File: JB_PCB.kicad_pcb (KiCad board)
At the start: 2 copper layers, 66 x 102.2 mm, 13 parts, among them J2 Screw_Terminal_01x02, J3 Screw_Terminal_01x02, J4 Screw_Terminal_01x02, J6 Screw_Terminal_01x02

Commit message: Added Servo pins
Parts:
- added J1: Conn_01x03_Pin, myFootprints.pretty-master:3x1_Pin_Header, F.Cu at (149.0, 141.2)
- added J5: Conn_01x03_Pin, myFootprints.pretty-master:3x1_Pin_Header, F.Cu at (152.5, 141.2)
- added J7: Conn_01x03_Pin, myFootprints.pretty-master:3x1_Pin_Header, F.Cu at (156.0, 141.2)
- added J8: Conn_01x03_Pin, myFootprints.pretty-master:3x1_Pin_Header, F.Cu at (159.5, 141.2)
- added J9: Conn_01x03_Pin, myFootprints.pretty-master:3x1_Pin_Header, F.Cu at (163.0, 141.2)
- moved REF** 13.6 mm to (159.5, 152.5)
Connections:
- A1 pad 10: unconnected-(A1-D7-Pad10) -> Net-(A1-D7)
- A1 pad 11: unconnected-(A1-D8-Pad11) -> Net-(A1-D8)
- A1 pad 16: unconnected-(A1-D13-Pad16) -> Net-(A1-D13)
- A1 pad 5: unconnected-(A1-D2-Pad5) -> Net-(A1-D2)
- A1 pad 7: unconnected-(A1-D4-Pad7) -> Net-(A1-D4)
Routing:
- net Net-(A1-D7): track 0.00 -> 83.6 mm
- net Net-(A1-D13): track 0.00 -> 81.9 mm, vias 0 -> 1
- net Net-(A1-D8): track 0.00 -> 73.9 mm, vias 0 -> 2
- net Net-(A1-VIN): track 37.6 -> 100.2 mm, vias 0 -> 1
- net Net-(A1-D4): track 0.00 -> 60.2 mm
- net Net-(A1-D2): track 0.00 -> 54.5 mm
- net Net-(ARD_PWR1-Pin_1): track 121.9 -> 164.6 mm
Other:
- board size 66 x 102.2 mm -> 66 x 114.2 mm
- board text added: "D13"
- board text added: "D2"
- board text added: "D4"
- board text added: "D7"
- board text added: "SIG"
- board text added: "TigerSharks R.O.V. CO"

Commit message: thickened traces
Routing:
- net Net-(J2-Pin_2): track 139.6 -> 145.7 mm
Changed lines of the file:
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@@
 		(descr "<B>WR-PHD </B><BR> 2.54mm Pin Header, 3 Pin")
 		(property "Reference" "J1"
-			(at -6.6096 -0.6625 270)
+			(at -6.6096 -0.6625 -90)
 			(layer "F.SilkS")
 			(hide yes)
@@
 		)
 		(property "Value" "Conn_01x03_Pin"
-			(at -8.968 1.0378 270)
+			(at -8.968 1.0378 -90)
 			(layer "F.Fab")
 			(effects
@@
 		(descr "<B>WR-PHD </B><BR> 2.54mm Pin Header, 3 Pin")
 		(property "Reference" "J8"
-			(at -6.6096 -0.6625 270)
+			(at -6.6096 -0.6625 -90)
 			(layer "F.SilkS")
 			(hide yes)
@@
 		)
 		(property "Value" "Conn_01x03_Pin"
-			(at -8.968 1.0378 270)
+			(at -8.968 1.0378 -90)
 			(layer "F.Fab")
 			(effects
@@
 		(descr "<B>WR-PHD </B><BR> 2.54mm Pin Header, 3 Pin")
 		(property "Reference" "J9"
-			(at -6.6096 -0.6625 270)
+			(at -6.6096 -0.6625 -90)
 			(layer "F.SilkS")
 			(hide yes)
@@
 		)
 		(property "Value" "Conn_01x03_Pin"
-			(at -8.968 1.0378 270)
+			(at -8.968 1.0378 -90)
 			(layer "F.Fab")
 			(effects
@@
 		(descr "<B>WR-PHD </B><BR> 2.54mm Pin Header, 3 Pin")
 		(property "Reference" "J5"
-			(at -6.6096 -0.6625 270)
+			(at -6.6096 -0.6625 -90)
 			(layer "F.SilkS")
 			(hide yes)
@@
 		)
 		(property "Value" "Conn_01x03_Pin"
-			(at -8.968 1.0378 270)
+			(at -8.968 1.0378 -90)
 			(layer "F.Fab")
 			(effects
@@
 		(descr "<B>WR-PHD </B><BR> 2.54mm Pin Header, 3 Pin")
 		(property "Reference" "J7"
-			(at -6.6096 -0.6625 270)
+			(at -6.6096 -0.6625 -90)
 			(layer "F.SilkS")
 			(hide yes)
@@
 		)
 		(property "Value" "Conn_01x03_Pin"
-			(at -8.968 1.0378 270)
+			(at -8.968 1.0378 -90)
 			(layer "F.Fab")
 			(effects
@@
 		(start 110.250004 131.25)
 		(end 110.25 131.25)
-		(width 0.8)
-		(layer "F.Cu")
-		(net 29)
-	)
-	(segment
-		(start 112 138.75)
-		(end 135.104898 138.75)
-		(width 0.8)
+		(width 3.81)
 		(layer "F.Cu")
 		(net 29)
@@
 		(start 109.5 131.25)
 		(end 109.5 109.75)
-		(width 0.8)
+		(width 3.81)
 		(layer "F.Cu")
 		(net 29)
@@
 		(start 115.5 81.500004)
 		(end 110.000004 87)
-		(width 0.8)
+		(width 3.81)
 		(layer "F.Cu")
 		(net 29)
@@
 		(start 109.5 65.250008)
 		(end 115.5 59.250008)
-		(width 0.8)
+		(width 3.81)
 		(layer "F.Cu")
 		(net 29)
@@
 		(start 115.5 103.645106)
 		(end 109.5 109.645106)
-		(width 0.8)
+		(width 3.81)
 		(layer "F.Cu")
 		(net 29)
@@
 		(start 109.5 109.75)
 		(end 109.5 87)
-		(width 0.8)
+		(width 3.81)
 		(layer "F.Cu")
 		(net 29)
@@
 		(start 109.5 132)
 		(end 109.5 131.25)
-		(width 0.8)
+		(width 3.81)
 		(layer "F.Cu")
 		(net 29)
 	)
 	(segment
-		(start 135.104898 138.75)
-		(end 140.854898 133)
-		(width 0.8)
+		(start 109.5 139.5)
+		(end 113.75 143.75)
+		(width 3.81)
 		(layer "F.Cu")
 		(net 29)
 	)
 	(segment
-		(start 109.5 132)
-		(end 109.5 136.25)
-		(width 0.8)
+		(start 113.75 143.75)
+		(end 130.104898 143.75)
+		(width 3.81)
 		(layer "F.Cu")
 		(net 29)
@@
 		(start 110.25 131.25)
 		(end 109.5 132)
-		(width 0.8)
+		(width 3.81)
 		(layer "F.Cu")
 		(net 29)
 	)
 	(segment
-		(start 109.5 136.25)
-		(end 112 138.75)
-		(width 0.8)
+		(start 130.104898 143.75)
+		(end 140.854898 133)
+		(width 3.81)
 		(layer "F.Cu")
 		(net 29)
@@
 		(start 110.000004 87)
 		(end 109.5 87)
-		(width 0.8)
+		(width 3.81)
 		(layer "F.Cu")
 		(net 29)
@@
 		(start 115.5 126.000004)
 		(end 110.250004 131.25)
-		(width 0.8)
+		(width 3.81)
 		(layer "F.Cu")
 		(net 29)
@@
 		(start 109.5 87)
 		(end 109.5 65.250008)
-		(width 0.8)
+		(width 3.81)
+		(layer "F.Cu")
+		(net 29)
+	)
+	(segment
+		(start 109.5 132)
+		(end 109.5 139.5)
+		(width 3.81)
 		(layer "F.Cu")
 		(net 29)
@@
 		(start 109.5 109.645106)
 		(end 109.5 109.75)
-		(width 0.8)
+		(width 3.81)
 		(layer "F.Cu")
 		(net 29)
@@
 		(start 125.75 133)
 		(end 118 133)
-		(width 0.8)
+		(width 3.81)
 		(layer "F.Cu")
 		(net 30)
@@
 		(start 125.75 133)
 		(end 121.25 128.5)
-		(width 0.8)
+		(width 3.81)
 		(layer "F.Cu")
 		(net 30)
@@
 		(start 121.25 71)
 		(end 119.000004 68.750004)
-		(width 0.8)
+		(width 3.81)
 		(layer "F.Cu")
 		(net 30)
@@
 		(start 119.000004 68.750004)
 		(end 115.5 68.750004)
-		(width 0.8)
+		(width 3.81)
 		(layer "F.Cu")
 		(net 30)
@@
 		(start 131.354902 133)
 		(end 125.75 133)
-		(width 0.8)
+		(width 3.81)
 		(layer "F.Cu")
 		(net 30)
@@
 		(start 119.145102 113.145102)
 		(end 121.25 115.25)
-		(width 0.8)
+		(width 3.81)
 		(layer "F.Cu")
 		(net 30)
@@
 		(start 121.25 115.25)
 		(end 121.25 128.5)
-		(width 0.8)
+		(width 3.81)
 		(layer "F.Cu")
 		(net 30)
@@
 		(start 115.5 91)
 		(end 119 91)
-		(width 0.8)
+		(width 3.81)
 		(layer "F.Cu")
 		(net 30)
@@
 		(start 121.25 71)
 		(end 121.25 93.25)
-		(width 0.8)
+		(width 3.81)
 		(layer "F.Cu")
 		(net 30)
@@
 		(start 121.25 93.25)
 		(end 121.25 115.25)
-		(width 0.8)
+		(width 3.81)
 		(layer "F.Cu")
 		(net 30)
@@
 		(start 115.5 113.145102)
 		(end 119.145102 113.145102)
-		(width 0.8)
+		(width 3.81)
 		(layer "F.Cu")
 		(net 30)
@@
 		(start 119 91)
 		(end 121.25 93.25)
-		(width 0.8)
+		(width 3.81)
 		(layer "F.Cu")
 		(net 30)
@@
 		(start 118 133)
 		(end 115.5 135.5)
-		(width 0.8)
+		(width 3.81)
 		(layer "F.Cu")
 		(net 30)

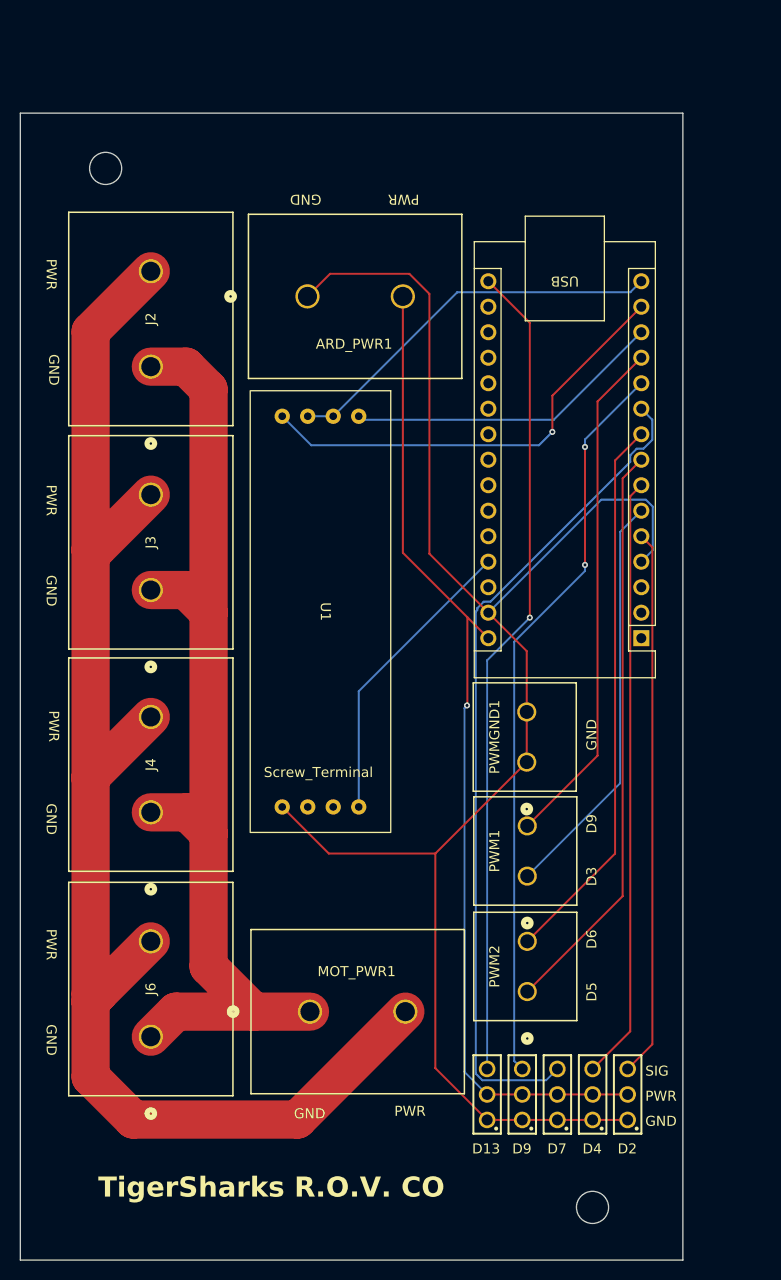
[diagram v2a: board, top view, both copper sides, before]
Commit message: added pins for external PWM board
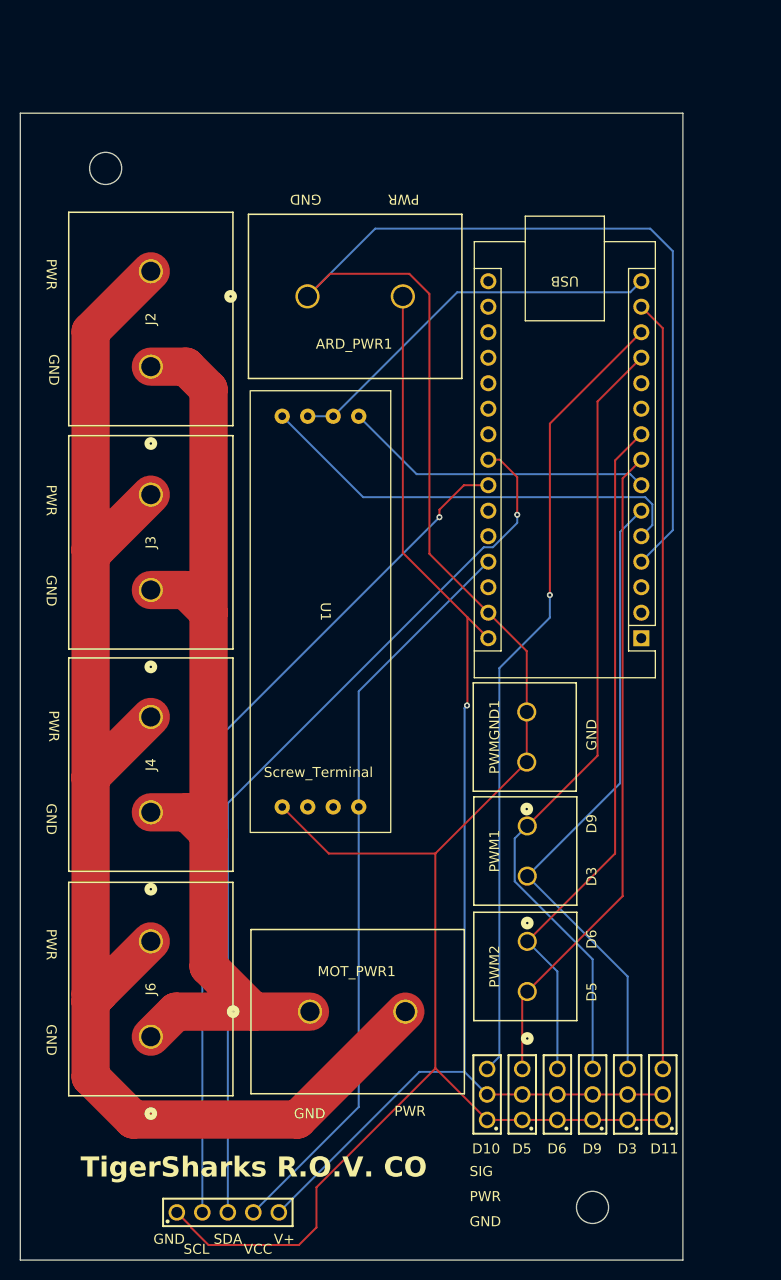
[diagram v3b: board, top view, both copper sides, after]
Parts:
- added J10: Conn_01x03_Pin, myFootprints.pretty-master:3x1_Pin_Header, F.Cu at (166.5, 141.2)
- added J12: Conn_01x05_Pin, myFootprints.pretty-master:1x5conn, F.Cu at (123.2, 153.0)
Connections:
- A1 pad 10: Net-(A1-D7) -> unconnected-(A1-D7-Pad10)
- A1 pad 11: Net-(A1-D8) -> unconnected-(A1-D8-Pad11)
- A1 pad 16: Net-(A1-D13) -> unconnected-(A1-D13-Pad16)
- A1 pad 23: unconnected-(A1-A4-Pad23) -> Net-(A1-A4)
- A1 pad 24: unconnected-(A1-A5-Pad24) -> Net-(A1-A5)
- J1 pad 3: Net-(A1-D13) -> Net-(A1-D10)
- J5 pad 3: Net-(A1-D8) -> Net-(A1-D5)
- J7 pad 3: Net-(A1-D7) -> Net-(A1-D6)
- J8 pad 3: Net-(A1-D4) -> Net-(A1-D9)
- J9 pad 3: Net-(A1-D2) -> Net-(A1-D3)
- U1 pad DI: Net-(A1-D11) -> Net-(A1-D2)
- U1 pad RO: Net-(A1-D10) -> Net-(A1-D4)
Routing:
- net Net-(A1-A4): track 0.00 -> 89.3 mm, vias 0 -> 1
- net Net-(A1-A5): track 0.00 -> 85.7 mm, vias 0 -> 1
- net Net-(ARD_PWR1-Pin_1): track 164.6 -> 250.0 mm
- net Net-(A1-D7): track 83.6 -> 0.00 mm
- net Net-(A1-D13): track 81.9 -> 0.00 mm, vias 1 -> 0
- net Net-(A1-D8): track 73.9 -> 0.00 mm, vias 2 -> 0
- net Net-(A1-D10): track 31.9 -> 79.8 mm, vias 0 -> 1
- net Net-(A1-+5V): track 29.8 -> 74.5 mm
- net Net-(A1-D11): track 44.8 -> 76.8 mm, vias 1 -> 0
- net Net-(A1-D4): track 60.2 -> 31.0 mm
- net Net-(A1-D9): track 51.3 -> 79.3 mm
- net Net-(A1-VIN): track 100.2 -> 128.0 mm
- net Net-(A1-D3): track 41.1 -> 64.5 mm
- net Net-(A1-D6): track 55.2 -> 69.2 mm
- net Net-(A1-D2): track 54.5 -> 44.1 mm
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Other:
- board text added: "D10"
- board text added: "D11"
- board text added: "SCL"
- board text added: "SDA"
- board text added: "V+"
- board text added: "VCC"
- board text removed: "D13"
- board text removed: "D2"
- board text removed: "D4"
- board text removed: "D7"

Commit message: changes from my laptop from last year
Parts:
- removed J10, J5, J7, J8, J9: Conn_01x03_Pin, myFootprints.pretty-master:3x1_Pin_Header
- removed J12: Conn_01x05_Pin, myFootprints.pretty-master:1x5conn
- removed PWM1, PWM2, PWMGND1: Screw_Terminal_01x02, myFootprints.pretty-master:screw 2x2
- added G***: LOGO, myFootprints.pretty-master:MateLogo, F.Cu at (142.5, 150.5)
- added REF**: CON6_1X6_TU_HTS_SAI, myFootprints.pretty-master:1x6Headers, F.Cu at (161.2, 144.0)
- J1: value Conn_01x03_Pin -> Conn_01x06_Pin; footprint myFootprints.pretty-master:3x1_Pin_Header -> myFootprints.pretty-master:1x6Headers
- moved J1 57.0 mm to (161.2, 85.5), turned to 0 degrees
- moved A1 17.9 mm to (165.0, 77.9)
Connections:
- A1 pad 11: unconnected-(A1-D8-Pad11) -> Net-(A1-D8)
- A1 pad 12: Net-(A1-D9) -> unconnected-(A1-D9-Pad12)
- A1 pad 13: Net-(A1-D10) -> unconnected-(A1-D10-Pad13)
- A1 pad 14: Net-(A1-D11) -> unconnected-(A1-D11-Pad14)
- A1 pad 16: unconnected-(A1-D13-Pad16) -> Net-(A1-D13)
- A1 pad 27: Net-(A1-+5V) -> Net-(A1-VIN)
- A1 pad 4: Net-(ARD_PWR1-Pin_1) -> unconnected-(A1-GND-Pad4)
- A1 pad 5: Net-(A1-D2) -> unconnected-(A1-D2-Pad5)
- A1 pad 6: Net-(A1-D3) -> unconnected-(A1-D3-Pad6)
- A1 pad 7: Net-(A1-D4) -> unconnected-(A1-D4-Pad7)
- A1 pad 8: Net-(A1-D5) -> unconnected-(A1-D5-Pad8)
- A1 pad 9: Net-(A1-D6) -> unconnected-(A1-D6-Pad9)
- J1 pad 2: Net-(A1-VIN) -> unconnected-(J1-Pin_2-Pad2)
- J1 pad 3: Net-(A1-D10) -> Net-(A1-A5)
- U1 pad DE: Net-(A1-D12) -> Net-(A1-D13)
- U1 pad DI: Net-(A1-D2) -> Net-(A1-D12)
- U1 pad RE: Net-(A1-D12) -> Net-(A1-D13)
- U1 pad RO: Net-(A1-D4) -> Net-(A1-D8)
- U1 pad VCC: Net-(A1-+5V) -> Net-(A1-VIN)
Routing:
- net Net-(ARD_PWR1-Pin_1): track 250.0 -> 102.2 mm, vias 0 -> 3
- net Net-(A1-D10): track 79.8 -> 0.00 mm, vias 1 -> 0
- net Net-(A1-D9): track 79.3 -> 0.00 mm
- net Net-(A1-D11): track 76.8 -> 0.00 mm
- net Net-(A1-+5V): track 74.5 -> 0.00 mm
- net Net-(A1-D6): track 69.2 -> 0.00 mm
- net Net-(A1-D5): track 65.6 -> 0.00 mm
- net Net-(A1-D3): track 64.5 -> 0.00 mm
- net Net-(A1-A4): track 89.3 -> 30.6 mm, vias 1 -> 3
- net Net-(A1-A5): track 85.7 -> 29.3 mm, vias 1 -> 3
- net Net-(A1-D8): track 0.00 -> 49.7 mm
- net Net-(J2-Pin_2): track 145.7 -> 194.8 mm
- net Net-(A1-D2): track 44.1 -> 0.00 mm
- net Net-(A1-D13): track 0.00 -> 41.6 mm
- net Net-(J2-Pin_1): track 100.7 -> 137.7 mm
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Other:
- board size 66 x 114.2 mm -> 73.8 x 123.5 mm
- board text removed: "D10"
- board text removed: "D11"
- board text removed: "D3"
- board text removed: "D5"
- board text removed: "D6"
- board text removed: "D9"
- board text removed: "SIG"
